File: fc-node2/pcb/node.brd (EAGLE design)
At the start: 50 x 24 mm, 15 parts, among them J1 AVR_SPI_PRG_62X3_LOCK

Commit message: put things in the right places
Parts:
- added C3: 100n, rcl:C0603
- added IC1: HTU21D, Mine:DFN6-L
- added R4, R5, R6: (no value), rcl:R0603
- U$1: value ATTINY13SOIC -> ATTINY84; device SparkFun-DigitalIC:SO08 -> SparkFun-DigitalIC:SO14
- moved U$3 4.34 mm to (10.2, 8.64)
- moved R2 3.64 mm to (10.4, 13.0)
- moved R1 3.54 mm to (8.64, 13.0)
- moved C1 2.90 mm to (16.8, 13.0), turned to 180 degrees
- moved U$1 1.30 mm to (16.5, 4.83), turned to 0 degrees
- moved R3 1.27 mm to (4.06, 3.81)
- moved J2 1.14 mm to (3.81, 19.3), turned to 0 degrees
- moved D1 1.05 mm to (9.65, 16.0)
- moved DF 1.02 mm to (3.56, 7.37)
- moved JP1 1.02 mm to (23.1, 21.1)
- moved J1 0.76 mm to (18.0, 20.6)
- moved SOLAR 0.25 mm to (9.14, 18.5)
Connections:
- removed net DET/SCK: J1.3, U$1.7, U$3.1, U$4.SCK
- new net DET: U$1.5, U$3.1
- new net DIO0: U$1.12, U$4.DIO0
- new net EN: R3.1, U$1.10, U$2.3
- new net N$6: U$1.6
- new net N$7: U$4.RESET
- new net SCK: IC1.6, J1.3, U$1.9, U$4.SCK
- new net VSENSE: R5.1, R6.2, U$1.13
- net GND: now also C3.2, IC1.2, R6.1, U$1.14; no longer U$1.4
- net MISO: now also U$1.8; no longer U$1.6
- net MOSI: now also IC1.1, U$1.7; no longer U$1.5
- net N$4: now also U$1.3; no longer R3.1, U$1.2, U$2.3
- net RESET: now also U$1.4; no longer U$1.1
- net RFM_SS: now also R4.1, U$1.11; no longer U$1.3
- net VBATT: now also R5.2
- net VCC: now also C3.1, IC1.5, R4.2, U$1.1; no longer U$1.8
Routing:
- net SCK: track 0.00 -> 49.6 mm, vias 0 -> 2
- net EN: track 0.00 -> 35.6 mm
- net DET/SCK: track 32.9 -> 0.00 mm, vias 1 -> 0
- net N$4: track 21.9 -> 0.00 mm
- net DIO0: track 0.00 -> 20.7 mm, vias 0 -> 1
- net RESET: track 44.3 -> 25.6 mm, vias 2 -> 0
- net VCC: track 45.5 -> 61.9 mm, vias 1 -> 0
- net DET: track 0.00 -> 16.0 mm
- net VBATT: track 22.2 -> 35.2 mm
- net MISO: track 31.4 -> 21.1 mm
- net MOSI: track 42.0 -> 49.9 mm, vias 1 -> 2
- net GND: track 2.09 -> 5.75 mm, vias 21 -> 32
- net RFM_SS: track 11.7 -> 9.28 mm
- net N$3: track 10.0 -> 8.58 mm
- net N$1: track 8.26 -> 6.92 mm
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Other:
- outline, holes or cut-outs redrawn
- board text added: "APR 15"
- board text added: "APRIL 2015"
- board text added: "JON"
- board text added: "JON SOWMAN"
- board text added: "SOWMAN"
- board text added: "UKHAS"
- board text added: "ukhas.net"
- board text removed: "MAR '15"
- board text removed: "UKHASNET"

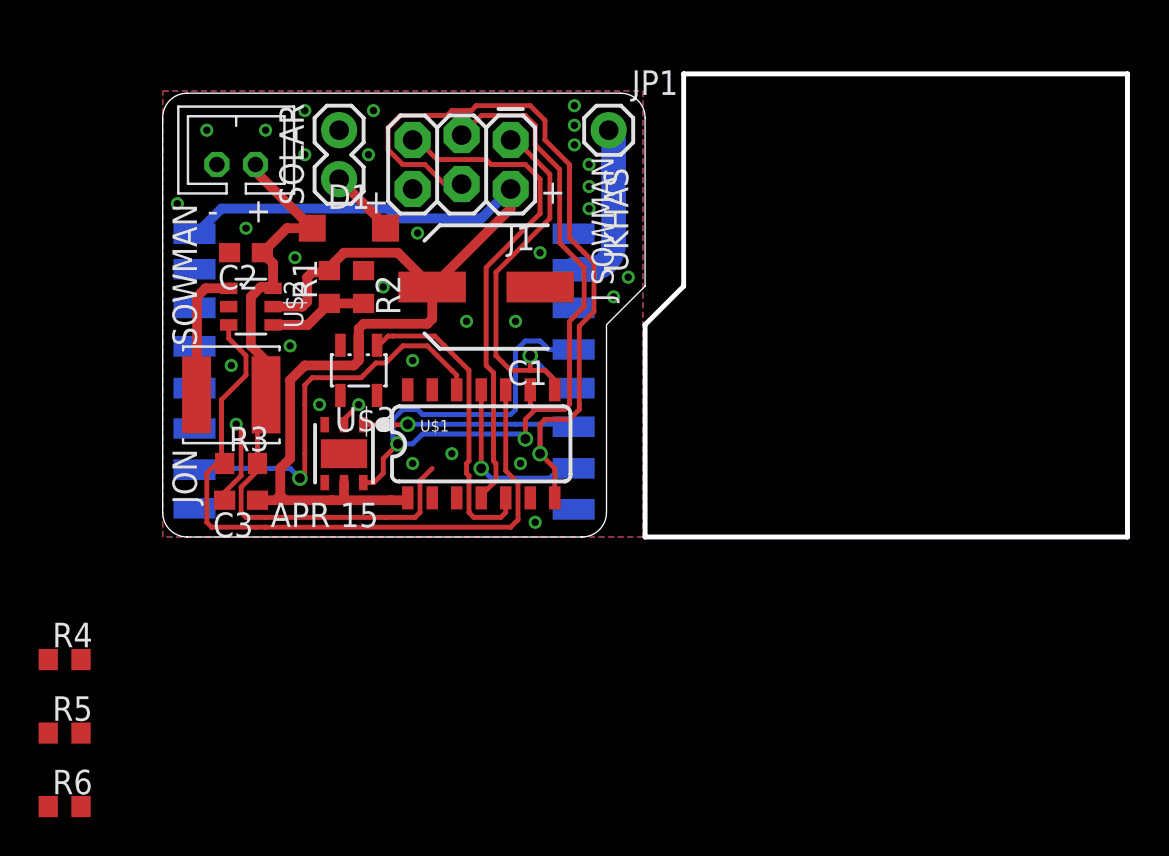
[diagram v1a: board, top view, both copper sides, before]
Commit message: adapt fc2 to take 80mah nimh button cells with solder tabs
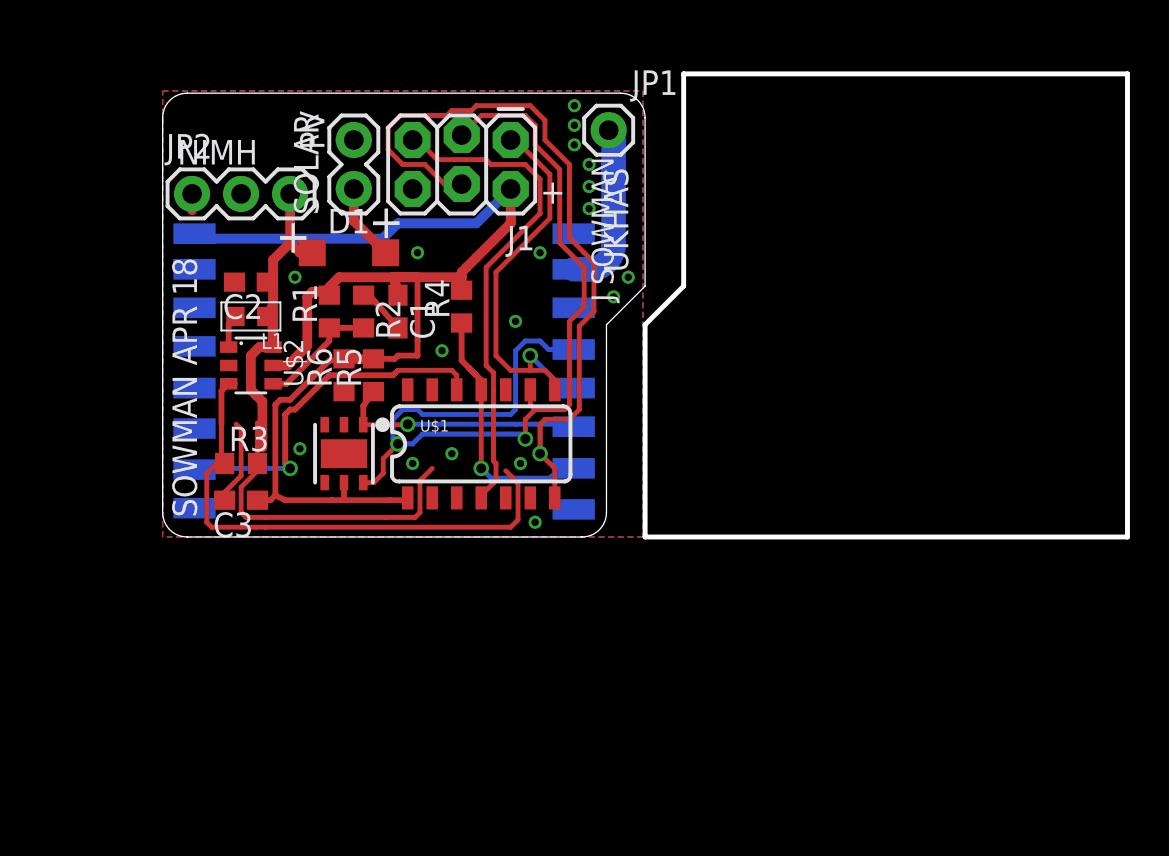
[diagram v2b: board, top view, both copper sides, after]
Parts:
- removed DF: 4u7, jonsowman:BOURNS_SRN5040_L
- removed J2: (no value), dtb:JST-2-TH
- removed U$3: BU49X_VDET_SOT235, jonsowman:SOT23-5L
- added JP2: (no value), SparkFun:1X03
- added L1: 4.7u, passives-7351:L0603-N
- C1: value 100u -> 4u7; device rcl:SANYO-OSCON_SMD_C6 -> rcl:C0603
- R5, R6: value (none) -> 4k7
- moved R4 27.5 mm to (15.5, 11.9), turned to 90 degrees
- moved R6 26.6 mm to (9.40, 8.38), turned to 90 degrees
- moved R5 24.5 mm to (10.9, 8.38), turned to 90 degrees
- moved C1 4.75 mm to (12.2, 11.7), turned to 270 degrees
- moved U$2 3.05 mm to (4.57, 8.89)
- moved C2 1.55 mm to (4.57, 13.2)
- moved R1 1.27 mm to (8.64, 11.7)
- moved R2 1.27 mm to (10.4, 11.7)
- moved D1 1.27 mm to (9.65, 14.7)
- moved SOLAR 0.92 mm to (9.91, 18.0)
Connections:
- removed net DET: U$1.5, U$3.1
- removed net VSENSE: R5.1, R6.2, U$1.13
- net EN: no longer U$1.10
- net GND: now also C1.2, JP2.1; no longer C1.-, J2.2, R6.1, U$3.3
- net MOSI: now also R5.1
- net N$1: now also L1.2; no longer DF.P$2
- net SCK: now also R6.1
- net VBATT: now also JP2.3, L1.1, U$1.13; no longer DF.P$1, J2.1, R5.2
- net VCC: now also C1.1, R5.2, R6.2; no longer C1.+, U$3.2
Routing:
- net DET: track 16.0 -> 0.00 mm
- net EN: track 35.6 -> 27.7 mm
- net N$1: track 6.92 -> 1.73 mm
- net RFM_SS: track 9.28 -> 13.7 mm
- net VCC: track 61.9 -> 65.8 mm
- net GND: track 5.75 -> 8.10 mm, vias 32 -> 18
- net MOSI: track 49.9 -> 51.8 mm
- net DIO0: track 20.7 -> 19.1 mm
- net VBATT: track 35.2 -> 36.7 mm
- net N$2: track 5.15 -> 6.29 mm
- net N$5: track 3.54 -> 4.37 mm
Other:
- board text added: "APRIL 2018"
- board text added: "NIMH"
- board text added: "PV"
- board text added: "SOWMAN APR 18"
- board text removed: "APR 15"
- board text removed: "APRIL 2015"
- board text removed: "JON"
- board text removed: "SOWMAN"
